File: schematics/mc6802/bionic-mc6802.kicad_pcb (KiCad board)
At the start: 2 copper layers, 27.9 x 68.6 mm, 9 parts, among them J1 Bionic-P135, J2 Bionic-P245, U1 MC6802P, U2 11AA010-I/TT

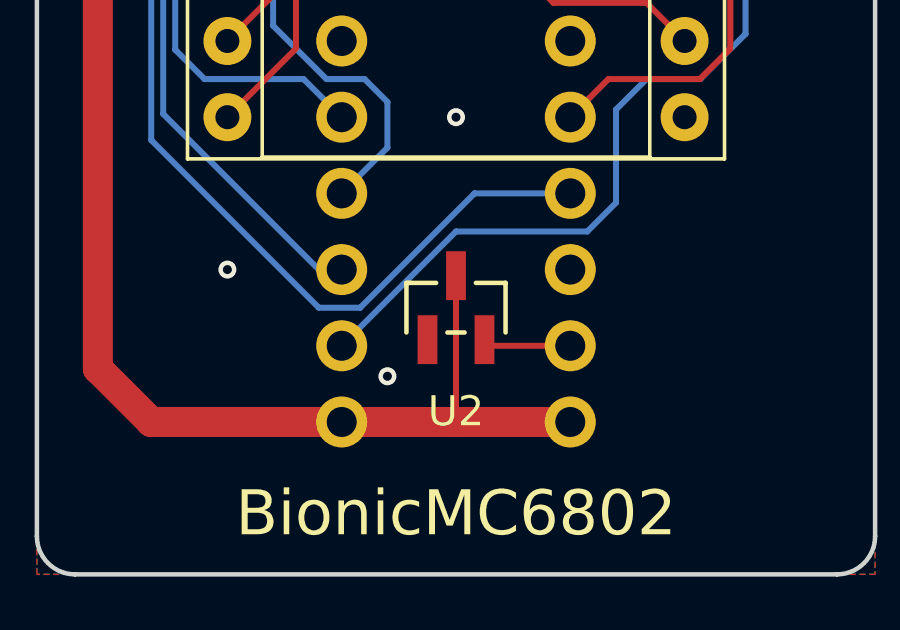
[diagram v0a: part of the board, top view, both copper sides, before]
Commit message: [MC6802] Fix EEPROM pinout
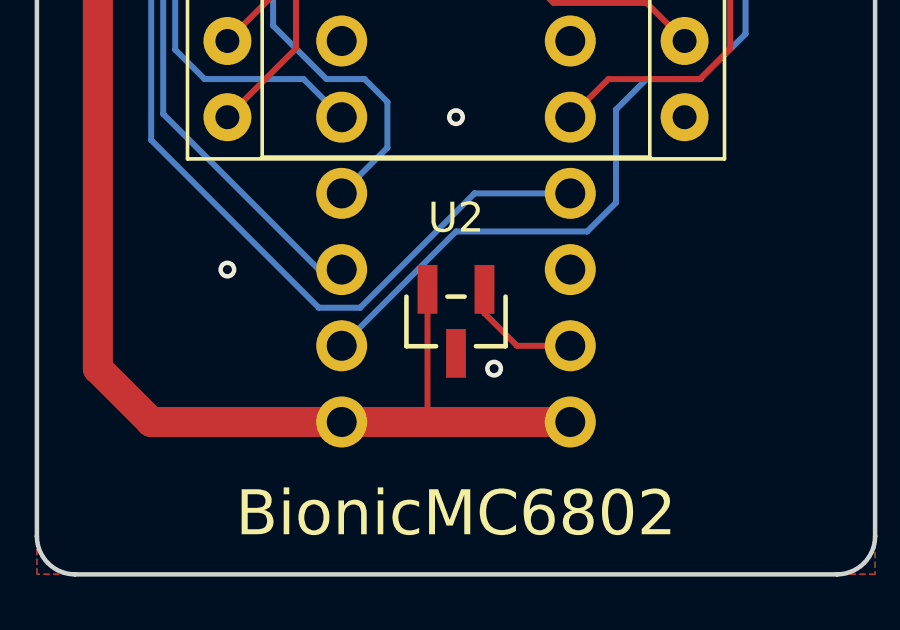
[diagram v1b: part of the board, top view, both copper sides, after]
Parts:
- moved U2 0.46 mm to (115.0, 130.1), turned to 180 degrees
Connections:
- U2 pad 1: GND -> Net-(J2-P57)
- U2 pad 2: Net-(J2-P57) -> VCC
- U2 pad 3: VCC -> GND
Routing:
- net Net-(J2-P57): track 2.94 -> 4.10 mm
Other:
- board text added: "Rev. 5"
- board text removed: "Rev. 4"
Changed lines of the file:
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@@
   (title_block
     (title "BionicMC6802")
-    (date "2024-03-16")
-    (rev "3")
+    (date "2024-11-01")
+    (rev "5")
     (company "Tadashi G. Takaoka")
   )
@@
   )
   (footprint "0-LocalLibrary:SOT-23_MC_MCH-M" (layer "F.Cu")
-    (at 114.97 129.69)
+    (at 114.97 130.148 180)
     (descr "Microchip 11AAxxx-I/TT UNI/O 1Kbit Serial EEPROM")
     (property "Sheetfile" "bionic-mc6802.kicad_sch")
@@
         (effects (font (size 1 1) (thickness 0.15)))
     )
-    (fp_text value "11AA010-I/TT" (at 0 0 unlocked) (layer "F.Fab")
+    (fp_text value "11AA010-I/TT" (at 0 0 180 unlocked) (layer "F.Fab")
         (effects (font (size 1 1) (thickness 0.15)))
     )
-    (fp_text user "${REFERENCE}" (at 0 0 unlocked) (layer "F.Fab")
+    (fp_text user "${REFERENCE}" (at 0 0 180 unlocked) (layer "F.Fab")
         (effects (font (size 1 1) (thickness 0.15)))
     )
@@
     (fp_circle (center -1.270999 0.446) (end -1.143999 0.446)
       (stroke (width 0.0254) (type solid)) (fill none) (layer "F.Fab"))
-    (pad "1" smd rect (at -0.950001 1.066) (size 0.6604 1.6256) (layers "F.Cu" "F.Paste" "F.Mask")
+    (pad "1" smd rect (at -0.950001 1.066 180) (size 0.6604 1.6256) (layers "F.Cu" "F.Paste" "F.Mask")
+      (net 40 "Net-(J2-P57)") (pinfunction "SCIO") (pintype "bidirectional"))
+    (pad "2" smd rect (at 0.950001 1.066 180) (size 0.6604 1.6256) (layers "F.Cu" "F.Paste" "F.Mask")
+      (net 1 "VCC") (pinfunction "VCC") (pintype "power_in"))
+    (pad "3" smd rect (at 0 -1.066 180) (size 0.6604 1.6256) (layers "F.Cu" "F.Paste" "F.Mask")
       (net 2 "GND") (pinfunction "VSS") (pintype "power_in"))
-    (pad "2" smd rect (at 0.950001 1.066) (size 0.6604 1.6256) (layers "F.Cu" "F.Paste" "F.Mask")
-      (net 40 "Net-(J2-P57)") (pinfunction "SCIO") (pintype "bidirectional"))
-    (pad "3" smd rect (at 0 -1.066) (size 0.6604 1.6256) (layers "F.Cu" "F.Paste" "F.Mask")
-      (net 1 "VCC") (pinfunction "VCC") (pintype "power_in"))
     (model "${KIPRJMOD}/0-LocalLibrary/SOT-23_MC_MCH.step"
       (offset (xyz 0 0 0))
@@
     (effects (font (size 0.8 0.8)) (justify bottom mirror))
   )
-  (gr_text "Rev. 4" (at 107.096 136.802) (layer "B.SilkS")
+  (gr_text "Rev. 5" (at 107.096 136.802) (layer "B.SilkS")
     (effects (font (size 1 1)) (justify left mirror))
   )
@@
     (effects (font (size 1 1) (thickness 0.15)) (justify right))
   )
+  (segment (start 113.954 133.5) (end 111.16 133.5) (width 1) (layer "F.Cu") (net 1))
   (segment (start 114.1953 76.35) (end 114.1953 71.778) (width 0.2) (layer "F.Cu") (net 1))
   (segment locked (start 103.286 92.86) (end 104.827 92.86) (width 1) (layer "F.Cu") (net 1))
   (segment (start 103.032 131.722) (end 104.81 133.5) (width 1) (layer "F.Cu") (net 1))
+  (segment (start 114.019999 133.434001) (end 113.954 133.5) (width 0.2) (layer "F.Cu") (net 1))
   (segment (start 103.032 93.114) (end 103.032 93.876) (width 1) (layer "F.Cu") (net 1))
-  (segment (start 114.97 133.5) (end 114.97 128.624) (width 0.2) (layer "F.Cu") (net 1))
+  (segment (start 114.97 133.5) (end 113.954 133.5) (width 1) (layer "F.Cu") (net 1))
   (segment (start 103.032 93.114) (end 103.032 92.7065) (width 0.2) (layer "F.Cu") (net 1))
   (segment (start 104.81 92.843) (end 104.81 92.7065) (width 0.2) (layer "F.Cu") (net 1))
-  (segment locked (start 114.97 133.5) (end 111.16 133.5) (width 1) (layer "F.Cu") (net 1))
   (segment locked (start 118.78 133.5) (end 114.97 133.5) (width 1) (layer "F.Cu") (net 1))
+  (segment (start 114.019999 129.082) (end 114.019999 133.434001) (width 0.2) (layer "F.Cu") (net 1))
   (segment locked (start 104.827 92.86) (end 107.35 92.86) (width 1) (layer "F.Cu") (net 1))
   (segment (start 103.032 93.876) (end 103.032 131.722) (width 1) (layer "F.Cu") (net 1))
@@
   (via (at 107.35 128.42) (size 0.6) (drill 0.3) (layers "F.Cu" "B.Cu") (free) (net 2))
   (via (at 114.97 123.34) (size 0.6) (drill 0.3) (layers "F.Cu" "B.Cu") (free) (net 2))
-  (via (at 112.684 131.976) (size 0.6) (drill 0.3) (layers "F.Cu" "B.Cu") (free) (net 2))
+  (via (at 116.24 131.722) (size 0.6) (drill 0.3) (layers "F.Cu" "B.Cu") (free) (net 2))
   (segment (start 119.344 127.15) (end 120.304 126.19) (width 0.2) (layer "B.Cu") (net 3))
   (segment (start 111.16 130.96) (end 114.97 127.15) (width 0.2) (layer "B.Cu") (net 3))
@@
   (segment (start 105.21 123.232) (end 110.398 128.42) (width 0.2) (layer "B.Cu") (net 38))
   (segment (start 105.21 82.3) (end 105.21 123.232) (width 0.2) (layer "B.Cu") (net 38))
-  (segment (start 118.78 130.96) (end 116.124 130.96) (width 0.2) (layer "F.Cu") (net 40))
-  (segment (start 116.124 130.96) (end 115.92 130.756) (width 0.2) (layer "F.Cu") (net 40))
+  (segment (start 117.002 130.96) (end 118.78 130.96) (width 0.2) (layer "F.Cu") (net 40))
+  (segment (start 115.920001 129.082) (end 115.920001 129.878001) (width 0.2) (layer "F.Cu") (net 40))
+  (segment (start 115.920001 129.878001) (end 117.002 130.96) (width 0.2) (layer "F.Cu") (net 40))
   (segment (start 124.114 121.054) (end 123.098 122.07) (width 0.2) (layer "F.Cu") (net 42))
   (segment (start 122.59 85.24) (end 124.114 86.764) (width 0.2) (layer "F.Cu") (net 42))

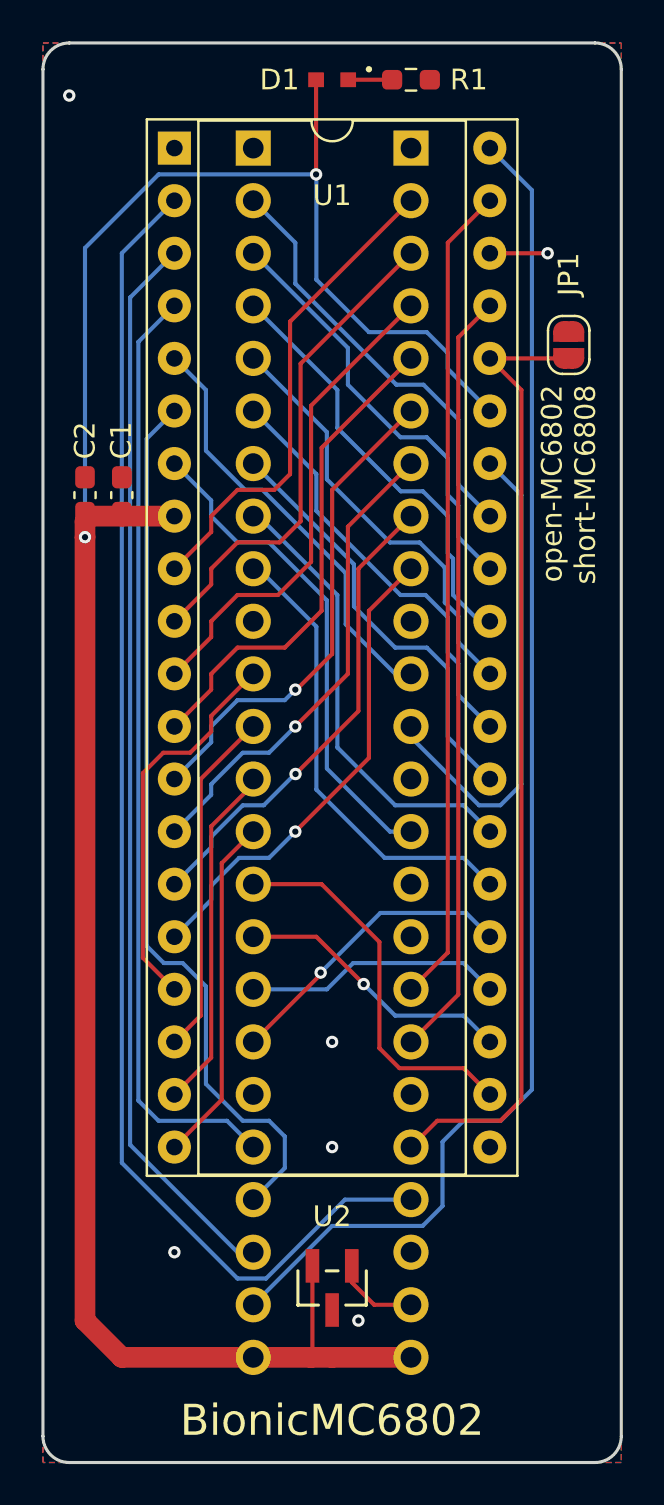
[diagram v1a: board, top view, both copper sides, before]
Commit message: [MC6802] Shrink board size
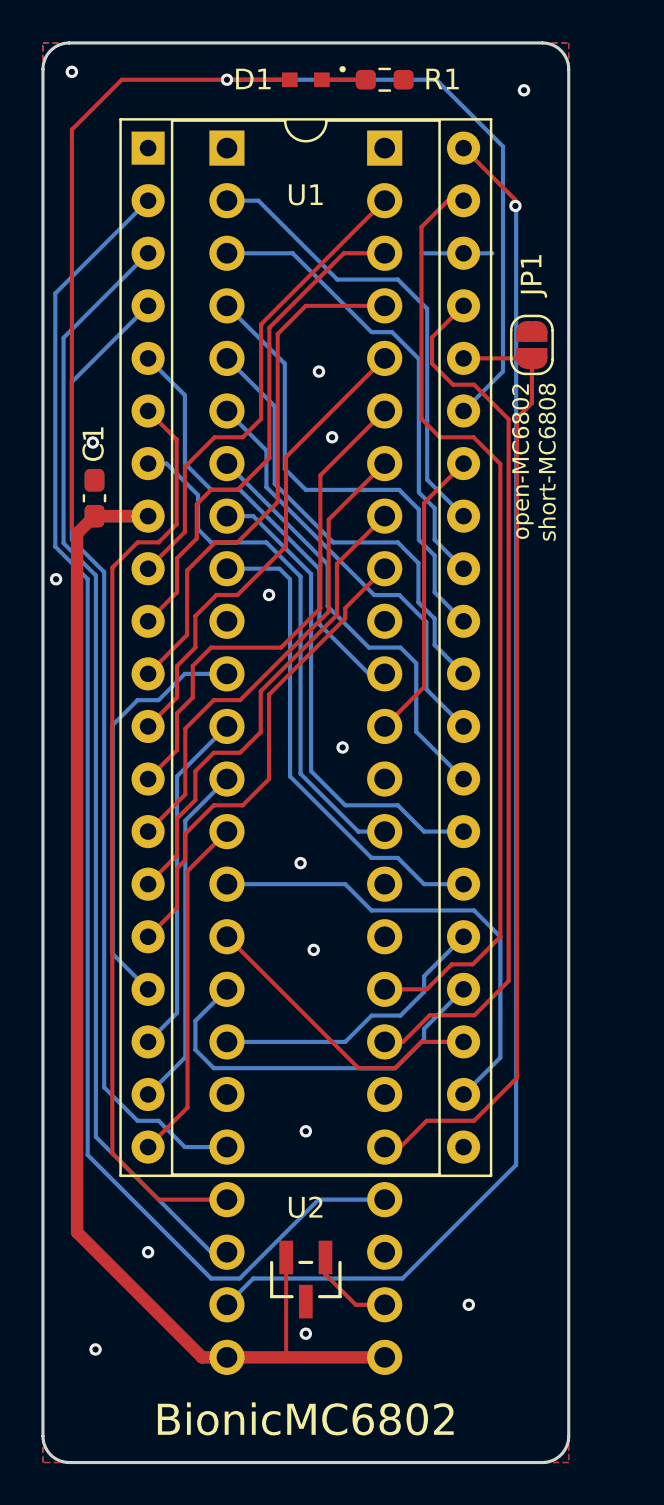
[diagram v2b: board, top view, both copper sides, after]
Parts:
- C2: moved to B.Cu
- moved JP1 1.78 mm to (124.6, 84.6)
- moved U2 1.33 mm to (113.7, 129.7)
- moved C1 1.33 mm to (103.5, 92.0)
- moved D1 1.27 mm to (113.7, 71.8)
- moved J1 1.27 mm to (109.9, 75.1)
- moved J2 1.27 mm to (117.5, 75.1)
- moved R1 1.27 mm to (117.5, 71.8)
- moved U1 1.27 mm to (106.1, 75.1)
- moved C2 0.48 mm to (103.5, 92.0)
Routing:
- net VCC: track 112.3 -> 122.0 mm, vias 2 -> 1
- net /P41: track 23.8 -> 14.3 mm
- net /P46: track 39.7 -> 46.0 mm
- net /P36: track 12.5 -> 18.8 mm
- net /P47: track 37.1 -> 42.6 mm
- net /P34: track 18.6 -> 22.6 mm
- net /P10: track 20.7 -> 22.6 mm
- net /P22: track 23.7 -> 25.4 mm
- net /P12: track 20.9 -> 22.6 mm
- net /P11: track 20.7 -> 22.4 mm
- net /P55: track 65.4 -> 67.0 mm
- net /P52: track 52.1 -> 53.7 mm
- net /P50: track 45.6 -> 47.1 mm
- net /P51: track 43.3 -> 44.8 mm
- net /P43: track 24.0 -> 25.3 mm
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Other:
- board size 27.9 x 68.6 mm -> 25.4 x 68.6 mm

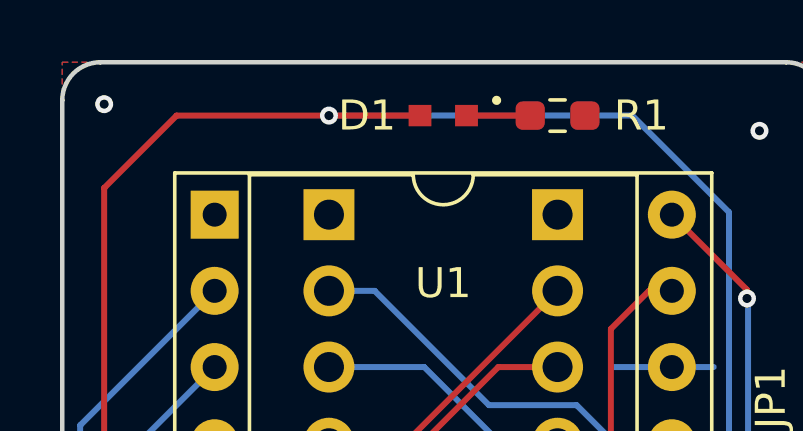
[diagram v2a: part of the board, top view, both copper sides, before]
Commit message: [schematics] Update LED footprint
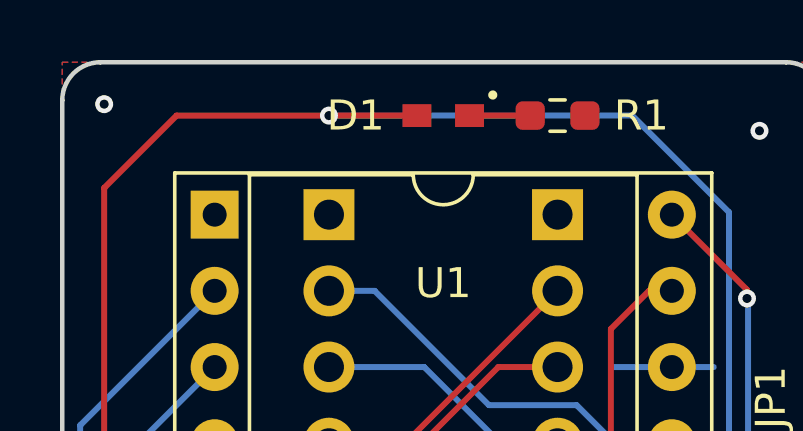
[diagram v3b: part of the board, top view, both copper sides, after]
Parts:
- D1: footprint 0-LocalLibrary:LED_CSL1901UW1_ROM -> 0-LocalLibrary:LED_CSL1901UW1_ROM-M
